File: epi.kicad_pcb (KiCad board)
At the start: 4 copper layers, 12.7 x 22.8 mm, 31 parts, among them J1 Connector 1x12, J2 Connector 1x12, J3 Conn_01x05, J4 USB-C 2.0 mid-mount female co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, U1 ATmega32U4-M, Y1 Crystal_GND24

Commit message: messing with outline and also spark gap
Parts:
- added E1: SparkGap, DIY:sparkgap_epi, F.Cu at (100.0, 57.9)
- moved C2 0.07 mm to (108.9, 64.9)
- moved C3 0.07 mm to (108.9, 69.0)
- moved J4 0.07 mm to (104.3, 53.3)
- moved R1 0.07 mm to (103.8, 59.0)
- moved R2 0.07 mm to (104.7, 59.0)
- moved R6 0.07 mm to (108.4, 61.6)
- moved R7 0.07 mm to (108.1, 70.8)
- moved R9 0.07 mm to (108.9, 63.0)
- moved RV2 0.07 mm to (102.9, 59.0)
- moved TP1 0.07 mm to (102.5, 58.8)
- moved TP2 0.07 mm to (106.1, 58.8)
- moved U1 0.07 mm to (104.3, 66.2)
- moved C10 0.07 mm to (106.6, 61.6)
- moved C4 0.07 mm to (103.3, 61.5)
- moved C5 0.07 mm to (106.3, 72.2)
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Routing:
- net GND: vias 10 -> 11
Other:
- outline, holes or cut-outs redrawn
- board text added: "Epi v1,2,2"
- board text removed: "Epi v1,2,1"

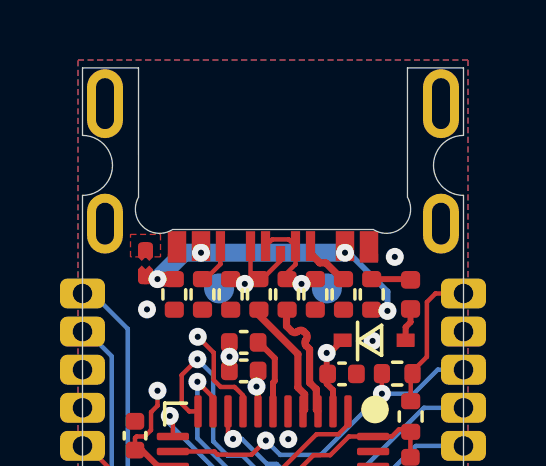
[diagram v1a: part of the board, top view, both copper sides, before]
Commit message: changed the method for inset corners to make space for the USB port
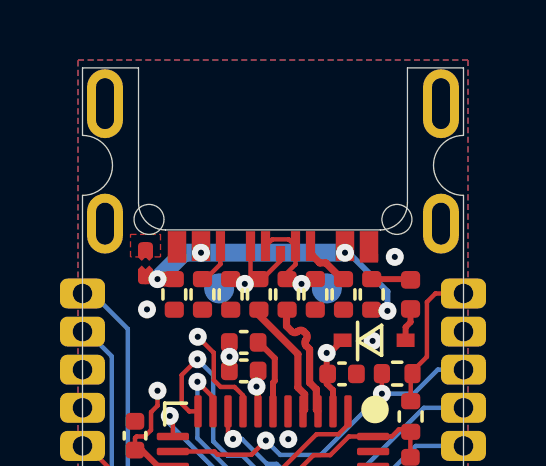
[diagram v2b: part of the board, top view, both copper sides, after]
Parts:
- added REF**: NPTH, DIY:NPTH, F.Cu at (108.4, 56.5)
- added REF**: NPTH, DIY:NPTH, F.Cu at (100.1, 56.5)
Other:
- outline, holes or cut-outs redrawn
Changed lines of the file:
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@@
     )
     (pad_to_mask_clearance 0)
-    (grid_origin 97.92322 0)
+    (grid_origin 108.754422 51.400001)
     (pcbplotparams
       (layerselection 0x00010fc_ffffffff)
@@
     )
   )
+  (footprint "DIY:NPTH" (layer "F.Cu")
+    (at 108.404422 56.450001)
+    (attr through_hole)
+    (fp_text reference "REF**" (at -0.05 -3.2 unlocked) (layer "F.SilkS") hide
+        (effects (font (size 1 1) (thickness 0.1)))
+    )
+    (fp_text value "NPTH" (at -0.1 2.2 unlocked) (layer "F.Fab")
+        (effects (font (size 1 1) (thickness 0.15)))
+    )
+    (fp_text user "${REFERENCE}" (at -0.1 3.7 unlocked) (layer "F.Fab")
+        (effects (font (size 1 1) (thickness 0.15)))
+    )
+    (pad "" np_thru_hole circle (at 0 0) (size 1 1) (drill 1) (layers "F&B.Cu" "*.Mask"))
+  )
   (footprint "Resistor_SMD:R_0402_1005Metric" (layer "F.Cu")
     (at 101.92322 58.95 90)
@@
     )
   )
+  (footprint "DIY:NPTH" (layer "F.Cu")
+    (at 100.140476 56.45)
+    (attr through_hole)
+    (fp_text reference "REF**" (at -0.05 -3.2 unlocked) (layer "F.SilkS") hide
+        (effects (font (size 1 1) (thickness 0.1)))
+    )
+    (fp_text value "NPTH" (at -0.1 2.2 unlocked) (layer "F.Fab")
+        (effects (font (size 1 1) (thickness 0.15)))
+    )
+    (fp_text user "${REFERENCE}" (at -0.1 3.7 unlocked) (layer "F.Fab")
+        (effects (font (size 1 1) (thickness 0.15)))
+    )
+    (pad "" np_thru_hole circle (at 0 0) (size 1 1) (drill 1) (layers "F&B.Cu" "*.Mask"))
+  )
   (footprint "Resistor_SMD:R_0402_1005Metric" (layer "F.Cu")
     (at 102.86322 58.95 -90)
@@
   (gr_line (start 104.411117 65.66537) (end 104.413821 65.6683)
     (stroke (width 0.18) (type solid)) (layer "B.SilkS"))
-  (gr_line (start 94.82322 57.3) (end 99.82322 57.3)
+  (gr_line (start 93.02322 57.3) (end 98.02322 57.3)
     (stroke (width 0.05588) (type default)) (layer "Dwgs.User"))
-  (gr_line (start 108.92322 57.3) (end 113.92322 57.3)
+  (gr_line (start 110.52322 57.3) (end 115.52322 57.3)
     (stroke (width 0.05588) (type default)) (layer "Dwgs.User"))
-  (gr_line (start 99.72322 77.3) (end 99.72322 72.3)
+  (gr_line (start 99.72322 79.1) (end 99.72322 74.1)
     (stroke (width 0.05588) (type default)) (layer "Dwgs.User"))
   (gr_line (start 110.62322 51.4) (end 110.62322 53.65)
@@
   (gr_line (start 97.92322 51.4) (end 97.92322 53.65)
     (stroke (width 0.01) (type solid)) (layer "Edge.Cuts"))
-  (gr_line (start 108.75522 55.708644) (end 108.754422 51.400001)
+  (gr_line (start 108.754422 55.900001) (end 108.754422 51.400001)
     (stroke (width 0.01) (type default)) (layer "Edge.Cuts"))
   (gr_arc (start 110.62322 55.65) (mid 109.62322 54.65) (end 110.62322 53.65)
     (stroke (width 0.01) (type solid)) (layer "Edge.Cuts"))
-  (gr_line (start 107.619247 56.786825) (end 100.927247 56.786824)
+  (gr_line (start 107.854422 56.800001) (end 100.690476 56.8)
+    (stroke (width 0.01) (type default)) (layer "Edge.Cuts"))
+  (gr_arc (start 100.690476 56.8) (mid 100.05408 56.536396) (end 99.790476 55.9)
     (stroke (width 0.01) (type default)) (layer "Edge.Cuts"))
-  (gr_line (start 99.791274 55.708643) (end 99.790476 51.4)
+  (gr_line (start 99.790476 55.9) (end 99.790476 51.4)
     (stroke (width 0.01) (type default)) (layer "Edge.Cuts"))
   (gr_arc (start 97.92322 53.65) (mid 98.92322 54.65) (end 97.92322 55.65)
@@
   (gr_line (start 110.62322 74.16) (end 110.62322 55.65)
     (stroke (width 0.01) (type solid)) (layer "Edge.Cuts"))
-  (gr_arc (start 108.75522 55.708644) (mid 108.610213 56.693368) (end 107.619247 56.786825)
-    (stroke (width 0.01) (type default)) (layer "Edge.Cuts"))
   (gr_line (start 97.92322 74.16) (end 110.62322 74.16)
     (stroke (width 0.01) (type solid)) (layer "Edge.Cuts"))
+  (gr_arc (start 108.754422 55.900001) (mid 108.490818 56.536397) (end 107.854422 56.800001)
+    (stroke (width 0.01) (type default)) (layer "Edge.Cuts"))
   (gr_line (start 97.92322 55.65) (end 97.92322 74.16)
     (stroke (width 0.01) (type solid)) (layer "Edge.Cuts"))
   (gr_line (start 97.92322 51.4) (end 99.790476 51.4)
     (stroke (width 0.01) (type solid)) (layer "Edge.Cuts"))
-  (gr_arc (start 100.927247 56.786824) (mid 99.93629 56.693376) (end 99.791274 55.708643)
-    (stroke (width 0.01) (type default)) (layer "Edge.Cuts"))
   (gr_line (start 113.72322 57.3) (end 113.72322 57.3)
     (stroke (width 0.1) (type default)) (layer "Edge.Cuts"))

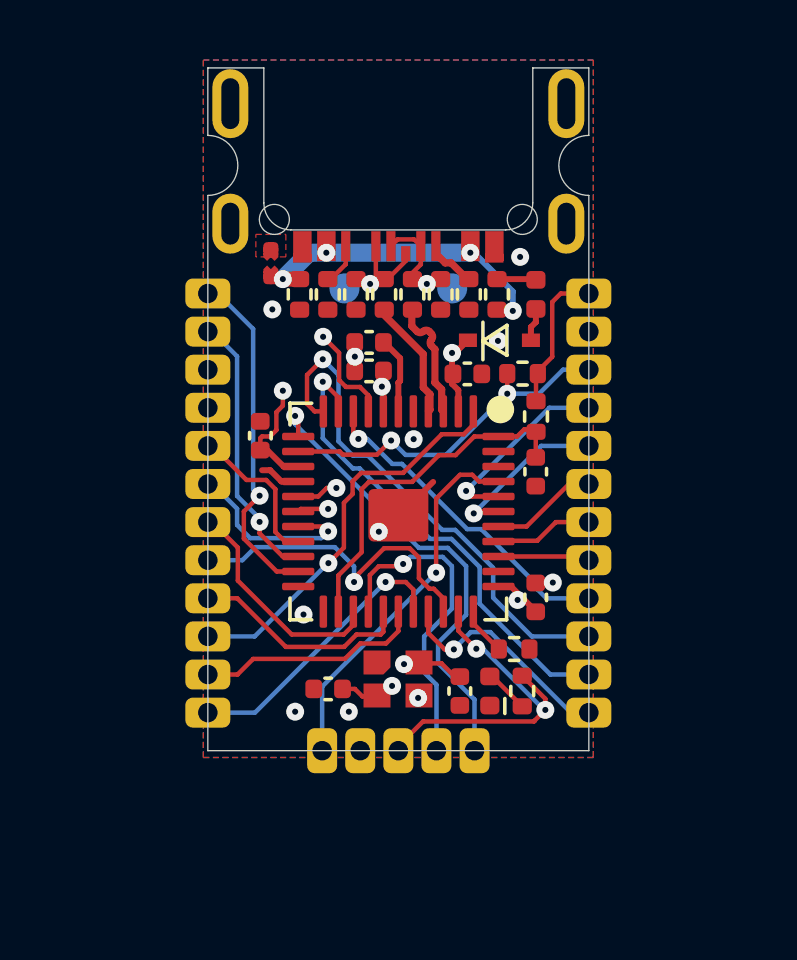
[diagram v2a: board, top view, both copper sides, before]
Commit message: USB shield connection set up
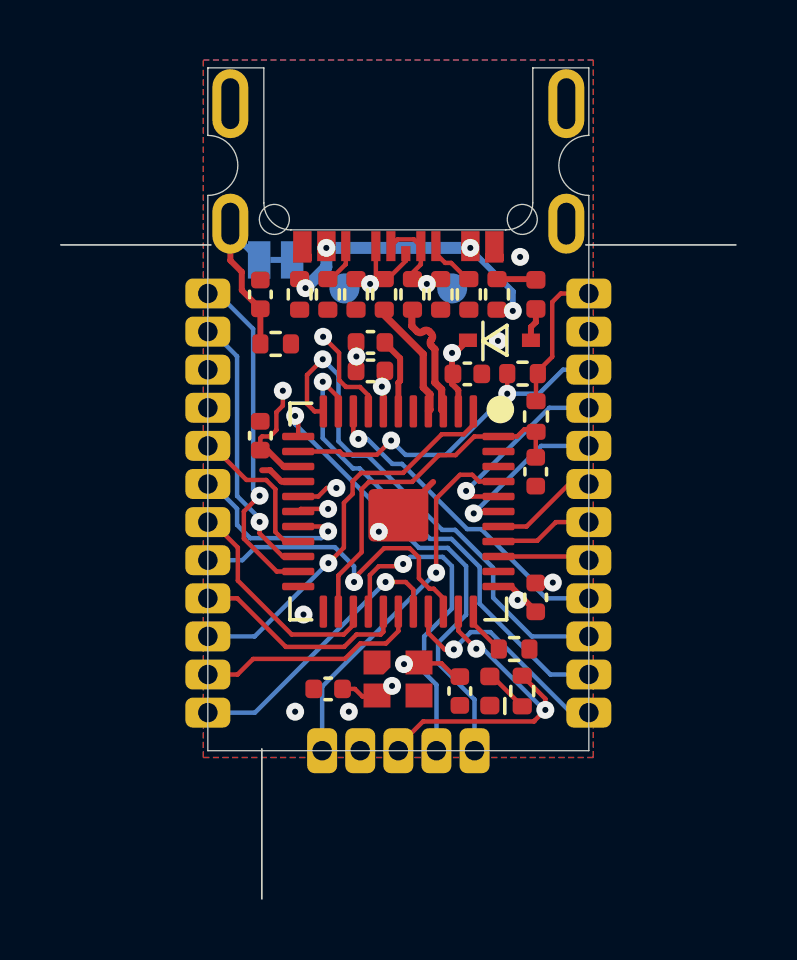
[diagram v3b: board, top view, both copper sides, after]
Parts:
- removed E1: SparkGap, DIY:sparkgap_epi
- added C1: 100nF, Capacitor_SMD:C_0402_1005Metric, F.Cu at (99.7, 59.0)
- added JP1: Jumper, Jumper:SolderJumper-2_P1.3mm_Bridged_RoundedPad1.0x1.5mm, B.Cu at (100.2, 57.8)
- added R3: 10kΩ, Resistor_SMD:R_0402_1005Metric, F.Cu at (100.2, 60.6)
- D2: footprint DIY:SOD323_bättre -> DIY:SOD323_bättre (2022_12_20 17_46_41 UTC)
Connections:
- J4 pad S1: unconnected-(J4-SHIELD-PadS1) -> Net-(J4-SHIELD)
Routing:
- net Net-(J4-SHIELD): track 0.00 -> 6.03 mm
- net Net-(FB1-Pad1): track 9.89 -> 9.09 mm
- net GND: track 2.98 -> 3.08 mm, vias 11 -> 8
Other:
- board size 12.7 x 22.8 mm -> 22.5 x 27.7 mm
- board text added: "Epi v1,2,4"
- board text removed: "Epi v1,2,2"

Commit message: Update epi.kicad_pcb
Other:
- board size 22.5 x 27.7 mm -> 12.7 x 22.8 mm
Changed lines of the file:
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@@
     (stroke (width 0.18) (type solid)) (layer "B.SilkS"))
   (gr_line (start 93.02322 57.3) (end 98.02322 57.3)
-    (stroke (width 0.05588) (type default)) (layer "Edge.Cuts"))
+    (stroke (width 0.05588) (type default)) (layer "Dwgs.User"))
+  (gr_line (start 110.52322 57.3) (end 115.52322 57.3)
+    (stroke (width 0.05588) (type default)) (layer "Dwgs.User"))
+  (gr_line (start 99.72322 79.1) (end 99.72322 74.1)
+    (stroke (width 0.05588) (type default)) (layer "Dwgs.User"))
   (gr_line (start 110.62322 51.4) (end 110.62322 53.65)
     (stroke (width 0.01) (type solid)) (layer "Edge.Cuts"))
   (gr_line (start 97.92322 51.4) (end 97.92322 53.65)
     (stroke (width 0.01) (type solid)) (layer "Edge.Cuts"))
-  (gr_line (start 110.52322 57.3) (end 115.52322 57.3)
-    (stroke (width 0.05588) (type default)) (layer "Edge.Cuts"))
   (gr_line (start 108.754422 55.900001) (end 108.754422 51.400001)
     (stroke (width 0.01) (type default)) (layer "Edge.Cuts"))
@@
   (gr_line (start 97.92322 51.4) (end 99.790476 51.4)
     (stroke (width 0.01) (type solid)) (layer "Edge.Cuts"))
-  (gr_line (start 99.72322 79.1) (end 99.72322 74.1)
-    (stroke (width 0.05588) (type default)) (layer "Edge.Cuts"))
   (gr_line (start 113.72322 57.3) (end 113.72322 57.3)
     (stroke (width 0.1) (type default)) (layer "Edge.Cuts"))

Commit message: big redesign
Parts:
- added C7: 10µF, Resistor_SMD:R_0402_1005Metric, F.Cu at (108.5, 59.0)
- C1, C10, C2, C3, C4, C5, C6, C8, C9: footprint Capacitor_SMD:C_0402_1005Metric -> Resistor_SMD:R_0402_1005Metric
- F1: footprint Fuse:Fuse_0402_1005Metric -> Resistor_SMD:R_0402_1005Metric
- moved R6 12.8 mm to (100.2, 71.4), turned to 90 degrees
- moved R9 7.91 mm to (101.1, 61.5), turned to 0 degrees
- moved R7 7.56 mm to (108.9, 63.2), turned to 90 degrees
- moved C3 7.46 mm to (101.7, 71.0), turned to 0 degrees
- moved C4 7.35 mm to (99.7, 67.8), turned to -90 degrees
- moved C2 6.77 mm to (103.0, 61.5), turned to 180 degrees
- moved C8 6.26 mm to (99.7, 65.6), turned to -90 degrees
- moved D2 2.25 mm to (105.4, 60.6)
- moved F1 1.88 mm to (108.0, 60.6), turned to 180 degrees
- moved C10 0.93 mm to (107.5, 61.6)
- moved C5 0.56 mm to (106.2, 71.6)
- moved R8 0.49 mm to (108.2, 71.7)
- moved D1 0.47 mm to (107.3, 71.7), turned to -90 degrees
- moved R3 0.24 mm to (100.3, 60.4)
- moved C6 0.21 mm to (101.9, 72.3)
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- renumbered REF** to DRILL1, REF** to DRILL2
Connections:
- D1 pad 1: GND -> Net-(D1-K)
- D1 pad 2: Net-(D1-A) -> D13
- R8 pad 1: D13 -> Net-(D1-K)
- R8 pad 2: Net-(D1-A) -> GND
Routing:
- net D17/SS: track 19.3 -> 11.3 mm, vias 1 -> 0
- net Net-(U1-XTAL2): track 11.8 -> 4.35 mm, vias 2 -> 0
- net D6: track 7.40 -> 14.8 mm, vias 0 -> 1
- net D4: track 7.62 -> 14.1 mm, vias 0 -> 1
- net Net-(U1-XTAL1): track 9.35 -> 3.07 mm, vias 2 -> 0
- net D2/SDA: track 5.17 -> 10.9 mm, vias 0 -> 1
- net D0/RX: track 9.14 -> 14.8 mm
- net D9: track 9.49 -> 14.9 mm
- net +5V: track 14.6 -> 19.9 mm, vias 4 -> 5
- net D8: track 7.60 -> 12.7 mm, vias 0 -> 1
- net RST: track 11.9 -> 17.0 mm
- net D11: track 15.7 -> 10.7 mm
- net A0: track 3.06 -> 7.88 mm, vias 0 -> 1
- net A2: track 3.60 -> 8.32 mm, vias 0 -> 1
- net A1: track 3.28 -> 7.99 mm, vias 0 -> 1
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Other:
- board text added: "Epi v1,3,0"
- board text removed: "Epi v1,2,4"

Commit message: little fix and updated gerbers
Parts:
- moved C10 0.46 mm to (108.0, 61.5)
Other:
- outline, holes or cut-outs redrawn
